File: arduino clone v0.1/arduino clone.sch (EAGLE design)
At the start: 7 parts, among them U101 ATMEGA328P_TQFP, U201 CH340G

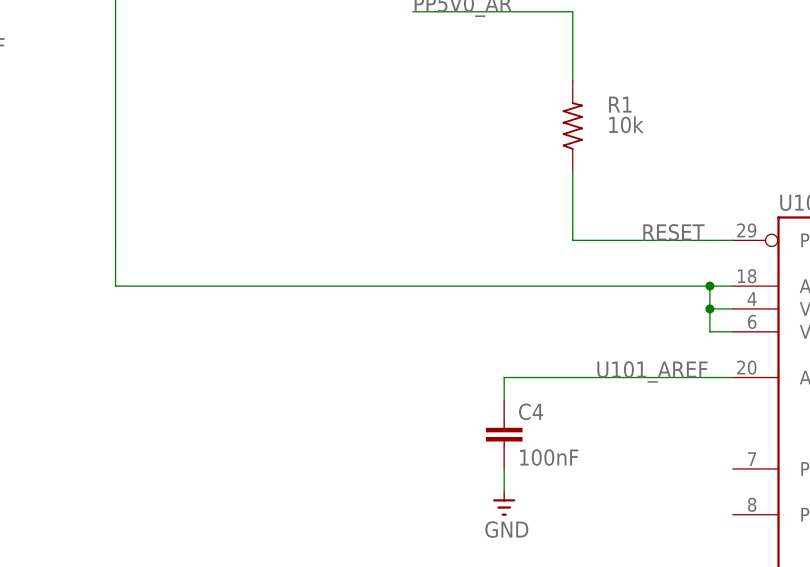
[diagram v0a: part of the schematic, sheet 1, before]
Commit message: add reset btn:
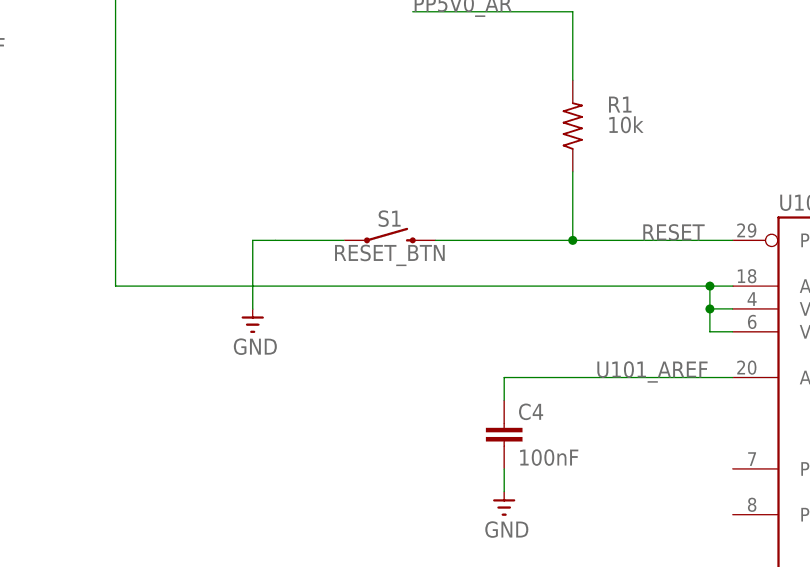
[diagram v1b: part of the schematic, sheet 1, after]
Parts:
- added S1: RESET_BTN, SparkFun-Switches:MOMENTARY-SWITCH-SPST-SMD-6.2MM-TALL
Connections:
- net GND: now also S1.1
- net RESET: now also S1.2
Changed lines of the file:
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@@
 <part name="C4" library="rcl" library_urn="urn:adsk.eagle:library:334" deviceset="C-EU" device="C0805" package3d_urn="urn:adsk.eagle:package:23617/2" value="100nF"/>
 <part name="GND5" library="supply" deviceset="GND" device=""/>
+<part name="S1" library="SparkFun-Switches" deviceset="MOMENTARY-SWITCH-SPST" device="-SMD-6.2MM-TALL" value="RESET_BTN"/>
+<part name="GND6" library="supply" deviceset="GND" device=""/>
 </parts>
 <sheets>
@@
 <instance part="GND5" gate="1" x="142.24" y="132.08" smashed="yes">
 <attribute name="VALUE" x="140.0175" y="129.54" size="1.778" layer="96"/>
+</instance>
+<instance part="S1" gate="G$1" x="129.54" y="162.56"/>
+<instance part="GND6" gate="1" x="114.3" y="152.4" smashed="yes">
+<attribute name="VALUE" x="112.0775" y="149.86" size="1.778" layer="96"/>
 </instance>
 </instances>
@@
 <wire x1="142.24" y1="134.62" x2="142.24" y2="137.16" width="0.1524" layer="91"/>
 </segment>
+<segment>
+<pinref part="GND6" gate="1" pin="GND"/>
+<wire x1="114.3" y1="154.94" x2="114.3" y2="162.56" width="0.1524" layer="91"/>
+<wire x1="114.3" y1="162.56" x2="116.84" y2="162.56" width="0.1524" layer="91"/>
+<pinref part="S1" gate="G$1" pin="1"/>
+<wire x1="116.84" y1="162.56" x2="124.46" y2="162.56" width="0.1524" layer="91"/>
+</segment>
 </net>
 <net name="RESET" class="0">
@@
 <wire x1="149.86" y1="162.56" x2="167.64" y2="162.56" width="0.1524" layer="91"/>
 <label x="157.48" y="162.56" size="1.778" layer="95"/>
+<pinref part="S1" gate="G$1" pin="2"/>
+<wire x1="134.62" y1="162.56" x2="149.86" y2="162.56" width="0.1524" layer="91"/>
+<junction x="149.86" y="162.56"/>
 </segment>
 </net>

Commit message: add custom CH340G symbol
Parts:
- removed U201: CH340G, Serial-Basic:CH340GSMD
- added U$1: CH340G, my-eagle-lib:CH340G
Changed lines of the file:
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@@
 <part name="U101" library="SparkFun-IC-Microcontroller" deviceset="ATMEGA328P_TQFP" device="" value="ATMEGA328P_TQFP"/>
 <part name="FRAME2" library="frames" library_urn="urn:adsk.eagle:library:229" deviceset="A3L-LOC" device=""/>
-<part name="U201" library="Serial-Basic" deviceset="CH340G" device="SMD" value="CH340G"/>
 <part name="GND3" library="supply" deviceset="GND" device=""/>
 <part name="C1" library="rcl" library_urn="urn:adsk.eagle:library:334" deviceset="C-EU" device="C0805" package3d_urn="urn:adsk.eagle:package:23617/2" value="4.7uF"/>
@@
 <part name="S1" library="SparkFun-Switches" deviceset="MOMENTARY-SWITCH-SPST" device="-SMD-6.2MM-TALL" value="RESET_BTN"/>
 <part name="GND6" library="supply" deviceset="GND" device=""/>
+<part name="U$1" library="my-eagle-lib" deviceset="CH340G" device=""/>
 </parts>
 <sheets>
@@
 <instances>
 <instance part="FRAME2" gate="G$1" x="0" y="0"/>
-<instance part="U201" gate="U1" x="170.18" y="134.62"/>
+<instance part="U$1" gate="G$1" x="185.42" y="124.46"/>
 </instances>
 <busses>
@@
 </drawing>
 <compatibility>
+<note version="6.3" minversion="6.2.2" severity="warning">
+Since Version 6.2.2 text objects can contain more than one line,
+which will not be processed correctly with this version.
+</note>
 <note version="8.2" severity="warning">
 Since Version 8.2, EAGLE supports online libraries. The ids

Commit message: add rail and rename CH340G
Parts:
- renumbered U$1 to U201
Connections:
- new net PP5V0_CH340G: U201.VCC
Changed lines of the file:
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@@
 <part name="S1" library="SparkFun-Switches" deviceset="MOMENTARY-SWITCH-SPST" device="-SMD-6.2MM-TALL" value="RESET_BTN"/>
 <part name="GND6" library="supply" deviceset="GND" device=""/>
-<part name="U$1" library="my-eagle-lib" deviceset="CH340G" device=""/>
+<part name="U201" library="my-eagle-lib" deviceset="CH340G" device=""/>
 </parts>
 <sheets>
@@
 <instances>
 <instance part="FRAME2" gate="G$1" x="0" y="0"/>
-<instance part="U$1" gate="G$1" x="185.42" y="124.46"/>
+<instance part="U201" gate="G$1" x="185.42" y="124.46"/>
 </instances>
 <busses>
 </busses>
 <nets>
+<net name="PP5V0_CH340G" class="0">
+<segment>
+<pinref part="U201" gate="G$1" pin="VCC"/>
+<wire x1="182.88" y1="185.42" x2="182.88" y2="218.44" width="0.1524" layer="91"/>
+<wire x1="182.88" y1="218.44" x2="109.22" y2="218.44" width="0.1524" layer="91"/>
+<label x="109.22" y="218.44" size="1.778" layer="95"/>
+</segment>
+</net>
 </nets>
 </sheet>

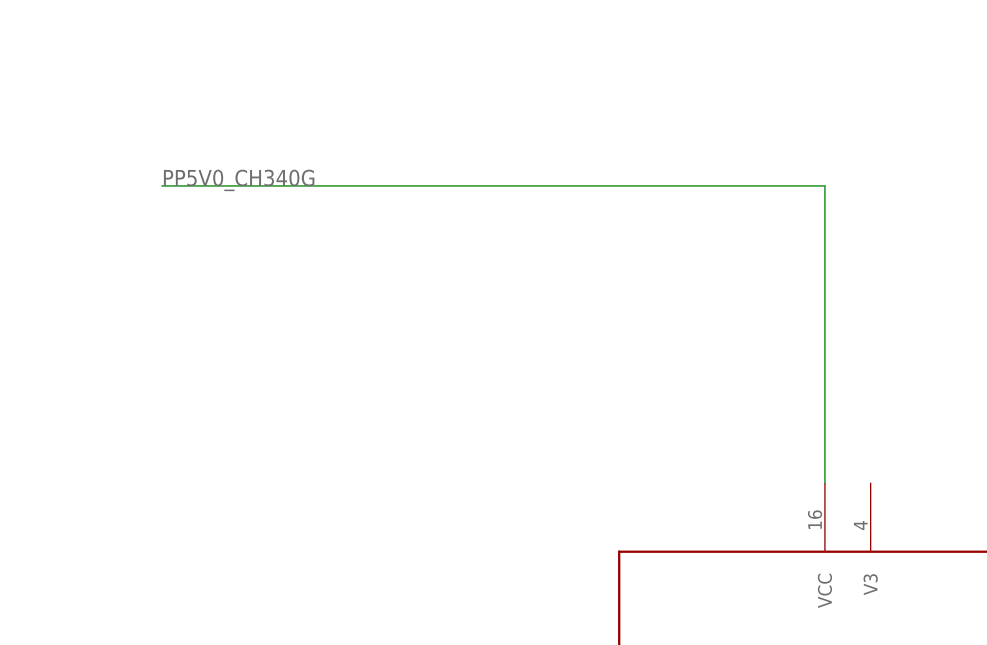
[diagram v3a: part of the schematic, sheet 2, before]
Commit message: add decoupling cap to 5V rail of CH340G
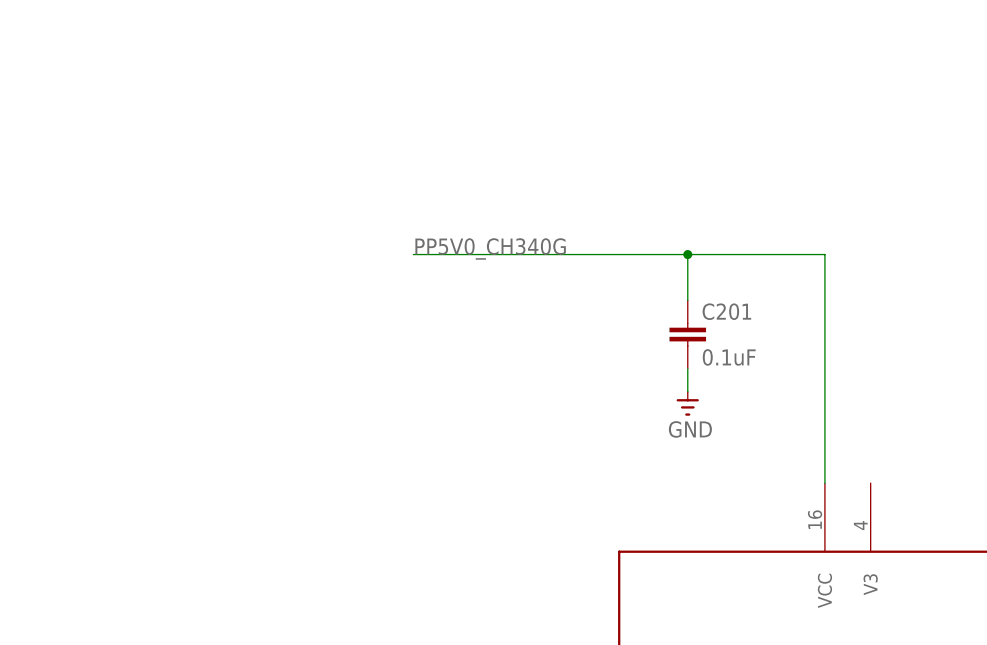
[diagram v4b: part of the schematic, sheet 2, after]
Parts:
- added C201: 0.1uF, rcl:C-EUC0805
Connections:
- net GND: now also C201.2
- net PP5V0_CH340G: now also C201.1
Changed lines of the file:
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@@
 <part name="GND6" library="supply" deviceset="GND" device=""/>
 <part name="U201" library="my-eagle-lib" deviceset="CH340G" device=""/>
+<part name="C201" library="rcl" library_urn="urn:adsk.eagle:library:334" deviceset="C-EU" device="C0805" package3d_urn="urn:adsk.eagle:package:23617/2" value="0.1uF"/>
+<part name="GND7" library="supply" deviceset="GND" device=""/>
 </parts>
 <sheets>
@@
 <instance part="FRAME2" gate="G$1" x="0" y="0"/>
 <instance part="U201" gate="G$1" x="185.42" y="124.46"/>
+<instance part="C201" gate="G$1" x="167.64" y="203.2"/>
+<instance part="GND7" gate="1" x="167.64" y="193.04" smashed="yes">
+<attribute name="VALUE" x="165.4175" y="190.5" size="1.778" layer="96"/>
+</instance>
 </instances>
 <busses>
@@
 <segment>
 <pinref part="U201" gate="G$1" pin="VCC"/>
-<wire x1="182.88" y1="185.42" x2="182.88" y2="218.44" width="0.1524" layer="91"/>
-<wire x1="182.88" y1="218.44" x2="109.22" y2="218.44" width="0.1524" layer="91"/>
-<label x="109.22" y="218.44" size="1.778" layer="95"/>
+<wire x1="182.88" y1="185.42" x2="182.88" y2="210.82" width="0.1524" layer="91"/>
+<wire x1="182.88" y1="210.82" x2="167.64" y2="210.82" width="0.1524" layer="91"/>
+<label x="137.16" y="210.82" size="1.778" layer="95"/>
+<pinref part="C201" gate="G$1" pin="1"/>
+<wire x1="167.64" y1="210.82" x2="137.16" y2="210.82" width="0.1524" layer="91"/>
+<wire x1="167.64" y1="205.74" x2="167.64" y2="210.82" width="0.1524" layer="91"/>
+<junction x="167.64" y="210.82"/>
 </segment>
 </net>
+<net name="GND" class="0">
+<segment>
+<pinref part="GND7" gate="1" pin="GND"/>
+<pinref part="C201" gate="G$1" pin="2"/>
+<wire x1="167.64" y1="195.58" x2="167.64" y2="198.12" width="0.1524" layer="91"/>
+</segment>
+</net>

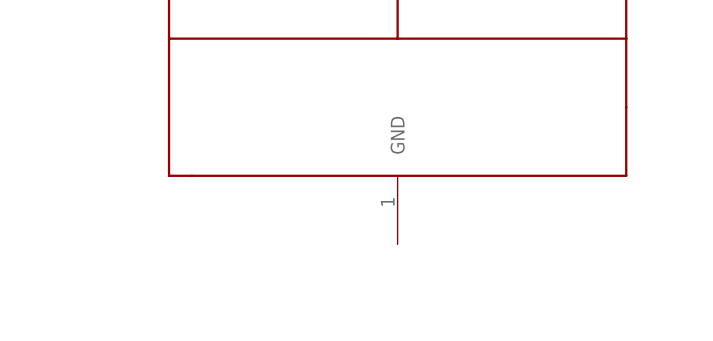
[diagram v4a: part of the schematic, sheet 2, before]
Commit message: connect gnd potential to CH340G
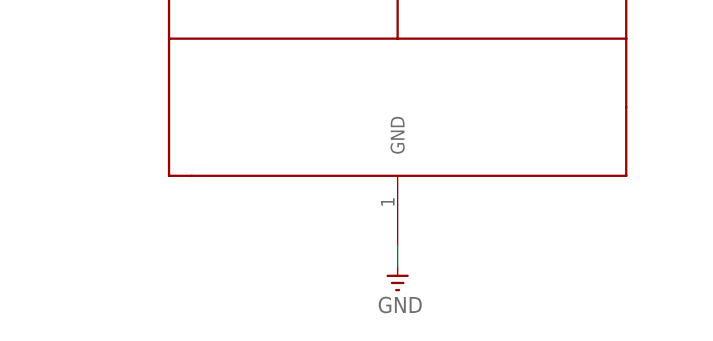
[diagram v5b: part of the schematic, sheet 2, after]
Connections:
- net GND: now also U201.GND
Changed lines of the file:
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@@
 <part name="C201" library="rcl" library_urn="urn:adsk.eagle:library:334" deviceset="C-EU" device="C0805" package3d_urn="urn:adsk.eagle:package:23617/2" value="0.1uF"/>
 <part name="GND7" library="supply" deviceset="GND" device=""/>
+<part name="GND8" library="supply" deviceset="GND" device=""/>
 </parts>
 <sheets>
@@
 <attribute name="VALUE" x="165.4175" y="190.5" size="1.778" layer="96"/>
 </instance>
+<instance part="GND8" gate="1" x="185.42" y="60.96" smashed="yes">
+<attribute name="VALUE" x="183.1975" y="58.42" size="1.778" layer="96"/>
+</instance>
 </instances>
 <busses>
@@
 <wire x1="167.64" y1="195.58" x2="167.64" y2="198.12" width="0.1524" layer="91"/>
 </segment>
+<segment>
+<pinref part="GND8" gate="1" pin="GND"/>
+<pinref part="U201" gate="G$1" pin="GND"/>
+<wire x1="185.42" y1="63.5" x2="185.42" y2="66.04" width="0.1524" layer="91"/>
+</segment>
 </net>

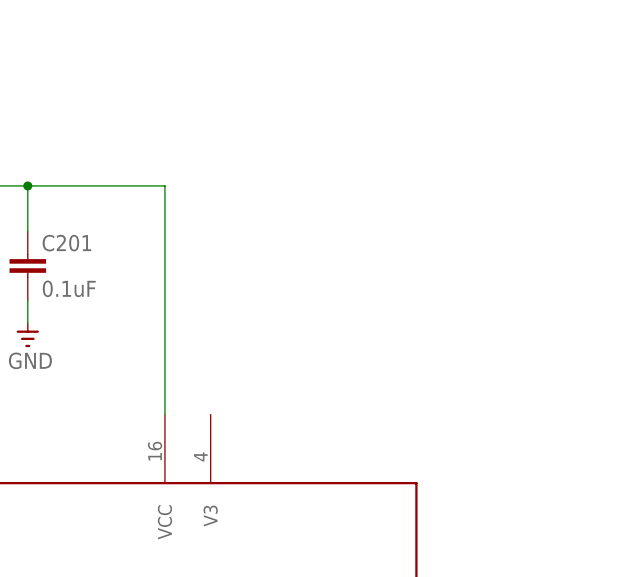
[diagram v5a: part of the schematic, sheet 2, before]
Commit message: add decoupling cap to PP3V3_CH340G rail
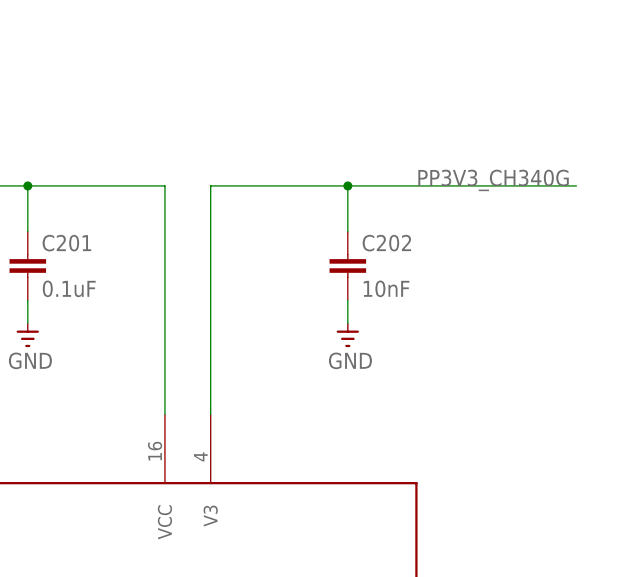
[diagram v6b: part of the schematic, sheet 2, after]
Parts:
- added C202: 10nF, rcl:C-EUC0805
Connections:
- new net PP3V3_CH340G: C202.1, U201.V3
- net GND: now also C202.2
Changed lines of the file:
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@@
 <part name="GND7" library="supply" deviceset="GND" device=""/>
 <part name="GND8" library="supply" deviceset="GND" device=""/>
+<part name="C202" library="rcl" library_urn="urn:adsk.eagle:library:334" deviceset="C-EU" device="C0805" package3d_urn="urn:adsk.eagle:package:23617/2" value="10nF"/>
+<part name="GND9" library="supply" deviceset="GND" device=""/>
 </parts>
 <sheets>
@@
 <attribute name="VALUE" x="183.1975" y="58.42" size="1.778" layer="96"/>
 </instance>
+<instance part="C202" gate="G$1" x="203.2" y="203.2"/>
+<instance part="GND9" gate="1" x="203.2" y="193.04" smashed="yes">
+<attribute name="VALUE" x="200.9775" y="190.5" size="1.778" layer="96"/>
+</instance>
 </instances>
 <busses>
@@
 <wire x1="185.42" y1="63.5" x2="185.42" y2="66.04" width="0.1524" layer="91"/>
 </segment>
-</net>
+<segment>
+<pinref part="GND9" gate="1" pin="GND"/>
+<pinref part="C202" gate="G$1" pin="2"/>
+<wire x1="203.2" y1="195.58" x2="203.2" y2="198.12" width="0.1524" layer="91"/>
+</segment>
+</net>
+<net name="PP3V3_CH340G" class="0">
+<segment>
+<pinref part="U201" gate="G$1" pin="V3"/>
+<wire x1="187.96" y1="185.42" x2="187.96" y2="210.82" width="0.1524" layer="91"/>
+<wire x1="187.96" y1="210.82" x2="203.2" y2="210.82" width="0.1524" layer="91"/>
+<label x="210.82" y="210.82" size="1.778" layer="95"/>
+<pinref part="C202" gate="G$1" pin="1"/>
+<wire x1="203.2" y1="210.82" x2="228.6" y2="210.82" width="0.1524" layer="91"/>
+<wire x1="203.2" y1="205.74" x2="203.2" y2="210.82" width="0.1524" layer="91"/>
+<junction x="203.2" y="210.82"/>
+</segment>
+</net>

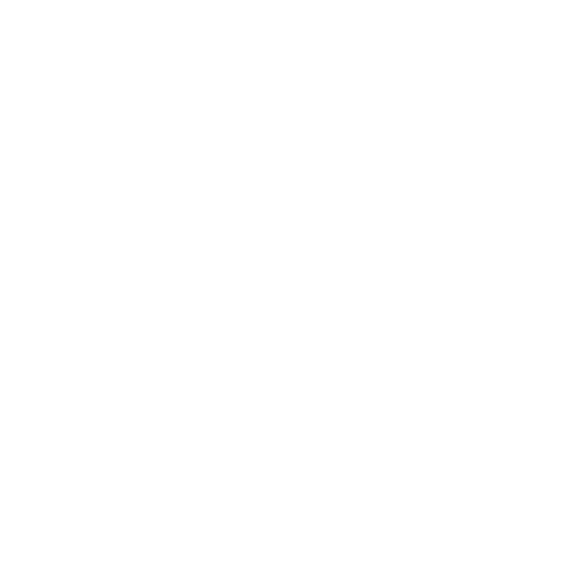
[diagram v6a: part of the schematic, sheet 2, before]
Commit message: add sparkfun micro USB port
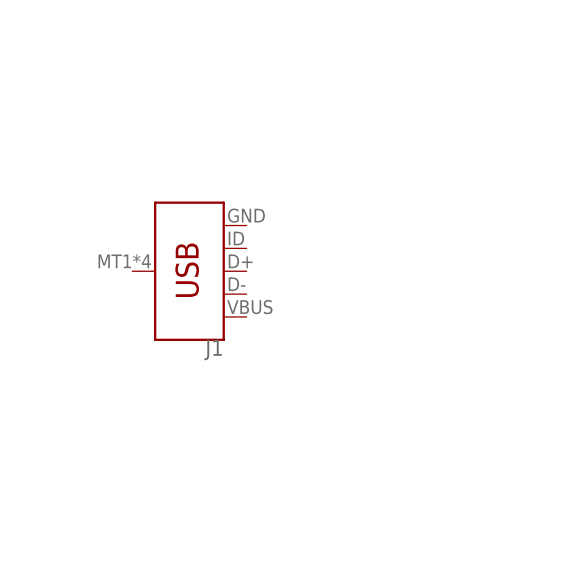
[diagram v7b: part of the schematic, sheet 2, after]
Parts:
- added J1: (no value), SparkFun-Connectors:USB_MICRO-B_SMT
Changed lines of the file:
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@@
 <part name="C202" library="rcl" library_urn="urn:adsk.eagle:library:334" deviceset="C-EU" device="C0805" package3d_urn="urn:adsk.eagle:package:23617/2" value="10nF"/>
 <part name="GND9" library="supply" deviceset="GND" device=""/>
+<part name="J1" library="SparkFun-Connectors" deviceset="USB_MICRO-B" device="_SMT"/>
 </parts>
 <sheets>
@@
 <attribute name="VALUE" x="200.9775" y="190.5" size="1.778" layer="96"/>
 </instance>
+<instance part="J1" gate="G$1" x="45.72" y="142.24" rot="R180"/>
 </instances>
 <busses>

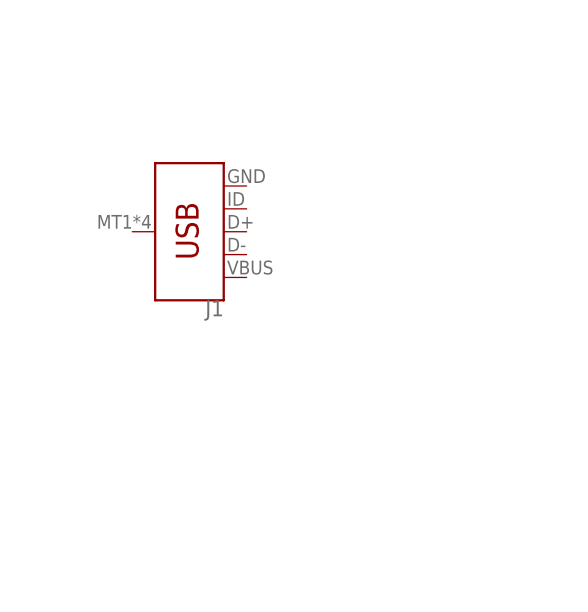
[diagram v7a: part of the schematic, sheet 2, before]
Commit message: swap out USB for one used in Arduino Sparkfun pro mini
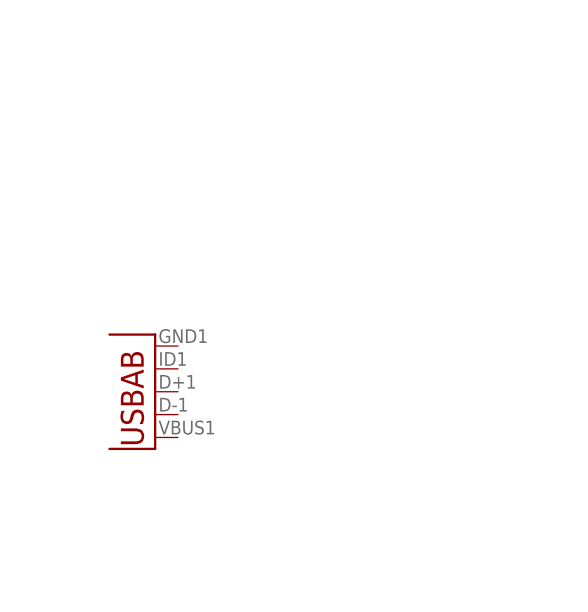
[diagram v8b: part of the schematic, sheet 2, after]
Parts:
- removed J1: (no value), SparkFun-Connectors:USB_MICRO-B_SMT
- added X1: (no value), Testing:USB-ABIN&OUT
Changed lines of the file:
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@@
 <part name="C202" library="rcl" library_urn="urn:adsk.eagle:library:334" deviceset="C-EU" device="C0805" package3d_urn="urn:adsk.eagle:package:23617/2" value="10nF"/>
 <part name="GND9" library="supply" deviceset="GND" device=""/>
-<part name="J1" library="SparkFun-Connectors" deviceset="USB_MICRO-B" device="_SMT"/>
+<part name="X1" library="Testing" deviceset="USB-AB" device="IN&amp;OUT"/>
 </parts>
 <sheets>
@@
 <attribute name="VALUE" x="200.9775" y="190.5" size="1.778" layer="96"/>
 </instance>
-<instance part="J1" gate="G$1" x="45.72" y="142.24" rot="R180"/>
+<instance part="X1" gate="G$1" x="38.1" y="124.46" rot="MR0"/>
 </instances>
 <busses>
